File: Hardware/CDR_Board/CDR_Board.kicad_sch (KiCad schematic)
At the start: 60 parts, among them J1 nRF52, J2 nRF24, J3 Battery, J4 GPIO & ADC, J5 USB_C_Receptacle_USB2.0, Q1 DMP2045U, SW1 BOOTSEL, SW2 RESET, SW3 SW_SPDT, U1 W25Q32JVSS, U2 AP2112, U3 RP2040, U4 BQ25172, U6 ADXL343, Y1 Crystal

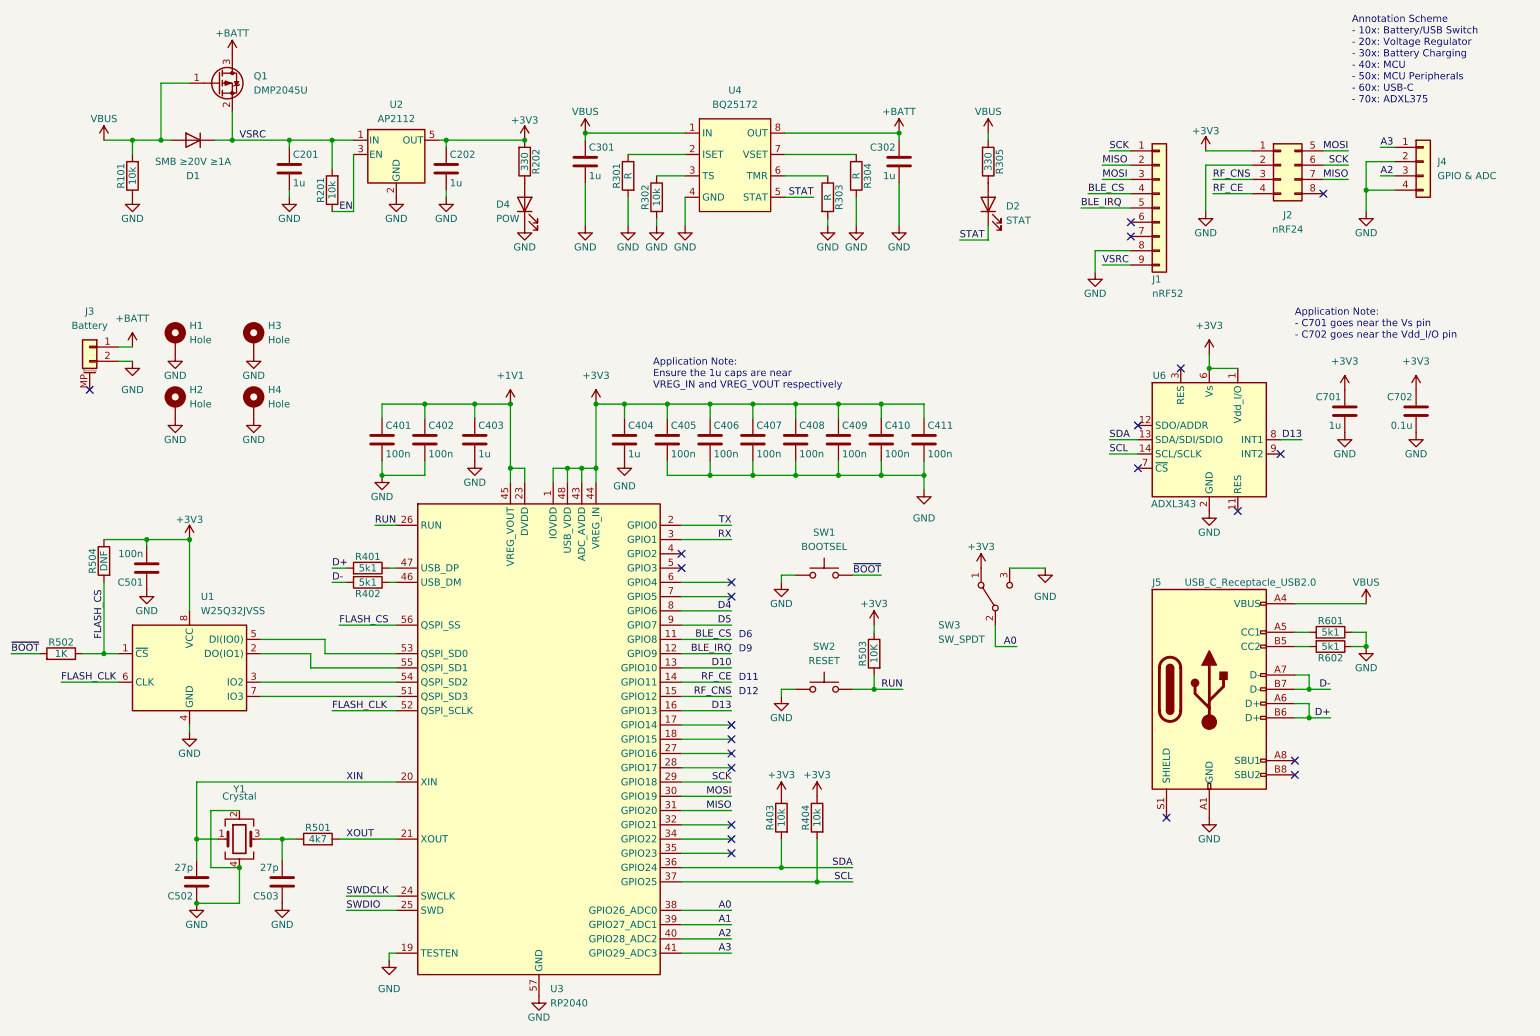
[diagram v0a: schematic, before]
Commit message: Added pullup/pulldown resistors for IMU
Added pullup resistor for CS, pulldown resistor for ADDR pin of IMU. Moved silkscreen
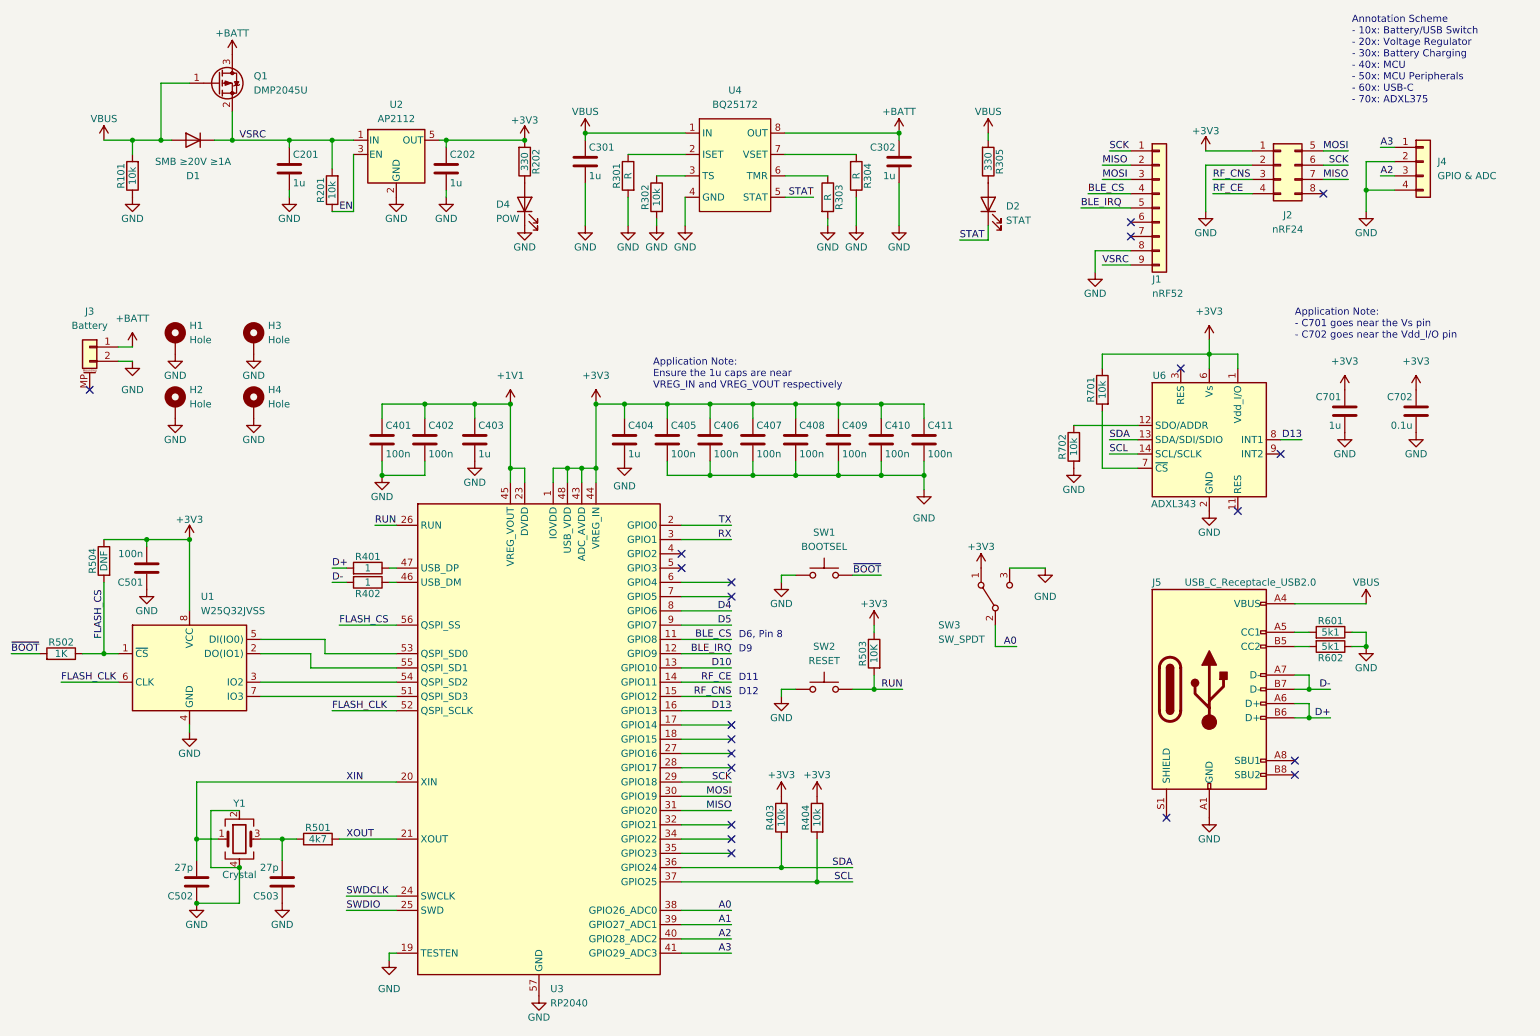
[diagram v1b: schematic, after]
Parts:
- added R701, R702: 10k, Resistor_SMD:R_0805_2012Metric_Pad1.20x1.40mm_HandSolder, symbol Device:R
- R401, R402: value 5k1 -> 1
- Y1: footprint Crystal:Crystal_SMD_0603-4Pin_6.0x3.5mm -> Crystal:Crystal_SMD_SeikoEpson_FA238-4Pin_3.2x2.5mm
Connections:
- net +3V3: now also R701.1
- net GND: now also R702.2
- net at U6.12 (SDO/ADDR): now also R702.1
- net at U6.7 (~{CS}): now also R701.2
- no-connect marks 23 -> 21
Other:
- note added: "D6, Pin 8"
- note removed: "D6"
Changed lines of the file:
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@@
   (junction (at 73.66 38.1) (diameter 0) (color 0 0 0 0)
   )
-  (junction (at 229.87 78.74) (diameter 0) (color 0 0 0 0)
-  )
   (junction (at 140.97 85.09) (diameter 0) (color 0 0 0 0)
   )
@@
   (junction (at 40.64 109.22) (diameter 0) (color 0 0 0 0)
   )
+  (junction (at 229.87 76.2) (diameter 0) (color 0 0 0 0)
+  )
   (junction (at 257.81 46.99) (diameter 0) (color 0 0 0 0)
   )
@@
   (no_connect (at 250.19 47.625))
   (no_connect (at 242.57 93.98))
-  (no_connect (at 217.17 96.52))
-  (no_connect (at 217.17 88.9))
   (no_connect (at 215.9 52.705))
   (no_connect (at 215.9 55.245))
@@
     (stroke (width 0) (type default) (color 0 0 0 0))
   )
+  (wire (pts (xy 210.82 86.36) (xy 210.82 96.52))
+    (stroke (width 0) (type default) (color 0 0 0 0))
+  )
   (wire (pts (xy 245.11 128.27) (xy 247.65 128.27))
     (stroke (width 0) (type default) (color 0 0 0 0))
@@
     (stroke (width 0) (type default) (color 0 0 0 0))
   )
+  (wire (pts (xy 217.17 96.52) (xy 210.82 96.52))
+    (stroke (width 0) (type default) (color 0 0 0 0))
+  )
   (wire (pts (xy 212.09 40.005) (xy 215.9 40.005))
     (stroke (width 0) (type default) (color 0 0 0 0))
@@
     (stroke (width 0) (type default) (color 0 0 0 0))
   )
-  (wire (pts (xy 229.87 78.74) (xy 234.95 78.74))
-    (stroke (width 0) (type default) (color 0 0 0 0))
-  )
   (wire (pts (xy 92.71 38.1) (xy 93.98 38.1))
     (stroke (width 0) (type default) (color 0 0 0 0))
@@
     (stroke (width 0) (type default) (color 0 0 0 0))
   )
+  (wire (pts (xy 210.82 76.2) (xy 229.87 76.2))
+    (stroke (width 0) (type default) (color 0 0 0 0))
+  )
   (wire (pts (xy 82.55 95.25) (xy 82.55 97.79))
     (stroke (width 0) (type default) (color 0 0 0 0))
@@
     (stroke (width 0) (type default) (color 0 0 0 0))
   )
+  (wire (pts (xy 234.95 76.2) (xy 229.87 76.2))
+    (stroke (width 0) (type default) (color 0 0 0 0))
+  )
   (wire (pts (xy 247.65 140.97) (xy 251.46 140.97))
     (stroke (width 0) (type default) (color 0 0 0 0))
   )
+  (wire (pts (xy 205.74 88.9) (xy 217.17 88.9))
+    (stroke (width 0) (type default) (color 0 0 0 0))
+  )
   (wire (pts (xy 257.81 46.99) (xy 257.81 41.91))
     (stroke (width 0) (type default) (color 0 0 0 0))
@@
     (stroke (width 0) (type default) (color 0 0 0 0))
   )
+  (wire (pts (xy 229.87 76.2) (xy 229.87 78.74))
+    (stroke (width 0) (type default) (color 0 0 0 0))
+  )
   (wire (pts (xy 171.45 85.09) (xy 179.07 85.09))
     (stroke (width 0) (type default) (color 0 0 0 0))
@@
     (stroke (width 0) (type default) (color 0 0 0 0))
   )
-  (wire (pts (xy 229.87 76.2) (xy 229.87 78.74))
+  (wire (pts (xy 229.87 73.66) (xy 229.87 76.2))
     (stroke (width 0) (type default) (color 0 0 0 0))
   )
@@
     (stroke (width 0) (type default) (color 0 0 0 0))
   )
+  (wire (pts (xy 234.95 78.74) (xy 234.95 76.2))
+    (stroke (width 0) (type default) (color 0 0 0 0))
+  )
   (wire (pts (xy 247.65 138.43) (xy 247.65 140.97))
     (stroke (width 0) (type default) (color 0 0 0 0))
   )
+  (wire (pts (xy 210.82 78.74) (xy 210.82 76.2))
+    (stroke (width 0) (type default) (color 0 0 0 0))
+  )
   (wire (pts (xy 60.96 137.16) (xy 85.09 137.16))
     (stroke (width 0) (type default) (color 0 0 0 0))
@@
     (stroke (width 0) (type default) (color 0 0 0 0))
   )
-  (text "D6" (at 146.05 127 0)
+  (text "D6, Pin 8\n" (at 146.05 127 0)
     (effects (font (size 1.27 1.27)) (justify left bottom))
   )
@@
     (in_bom yes) (on_board yes)
     (property "Reference" "R402" (id 0) (at 80.01 118.872 90))
-    (property "Value" "5k1" (id 1) (at 80.01 116.84 90))
+    (property "Value" "1" (id 1) (at 80.01 116.84 90))
     (property "Footprint" "Resistor_SMD:R_0805_2012Metric_Pad1.20x1.40mm_HandSolder" (id 2) (at 80.01 115.062 90)
       (effects (font (size 1.27 1.27)) hide)
@@
     (pin "1")
   )
+  (symbol (lib_id "Device:R") (at 210.82 82.55 0) (mirror y) (unit 1)
+    (in_bom yes) (on_board yes)
+    (property "Reference" "R701" (id 0) (at 208.788 82.55 90))
+    (property "Value" "10k" (id 1) (at 210.82 82.55 90))
+    (property "Footprint" "Resistor_SMD:R_0805_2012Metric_Pad1.20x1.40mm_HandSolder" (id 2) (at 212.598 82.55 90)
+      (effects (font (size 1.27 1.27)) hide)
+    )
+    (property "Datasheet" "~" (id 3) (at 210.82 82.55 0)
+      (effects (font (size 1.27 1.27)) hide)
+    )
+    (pin "1")
+    (pin "2")
+  )
   (symbol (lib_id "power:GND") (at 83.82 184.15 0) (unit 1)
     (in_bom yes) (on_board yes) (fields_autoplaced)
@@
     (pin "1")
   )
+  (symbol (lib_id "power:GND") (at 205.74 96.52 0) (mirror y) (unit 1)
+    (in_bom yes) (on_board yes)
+    (property "Reference" "#PWR025" (id 0) (at 205.74 102.87 0)
+      (effects (font (size 1.27 1.27)) hide)
+    )
+    (property "Value" "GND" (id 1) (at 205.74 100.33 0))
+    (property "Footprint" "" (id 2) (at 205.74 96.52 0)
+      (effects (font (size 1.27 1.27)) hide)
+    )
+    (property "Datasheet" "" (id 3) (at 205.74 96.52 0)
+      (effects (font (size 1.27 1.27)) hide)
+    )
+    (pin "1")
+  )
   (symbol (lib_id "Device:R") (at 33.02 113.03 0) (mirror y) (unit 1)
     (in_bom yes) (on_board yes)
@@
   (symbol (lib_id "Device:Crystal_GND24") (at 57.15 162.56 0) (unit 1)
     (in_bom yes) (on_board yes)
-    (property "Reference" "Y1" (id 0) (at 57.15 153.67 0))
-    (property "Value" "Crystal" (id 1) (at 57.15 154.94 0))
-    (property "Footprint" "Crystal:Crystal_SMD_0603-4Pin_6.0x3.5mm" (id 2) (at 57.15 162.56 0)
+    (property "Reference" "Y1" (id 0) (at 57.15 156.21 0))
+    (property "Value" "Crystal" (id 1) (at 57.15 168.91 0))
+    (property "Footprint" "Crystal:Crystal_SMD_SeikoEpson_FA238-4Pin_3.2x2.5mm" (id 2) (at 57.15 162.56 0)
       (effects (font (size 1.27 1.27)) hide)
     )
@@
     (in_bom yes) (on_board yes)
     (property "Reference" "R401" (id 0) (at 80.01 112.268 90))
-    (property "Value" "5k1" (id 1) (at 80.01 114.3 90))
+    (property "Value" "1" (id 1) (at 80.01 114.3 90))
     (property "Footprint" "Resistor_SMD:R_0805_2012Metric_Pad1.20x1.40mm_HandSolder" (id 2) (at 80.01 116.078 90)
       (effects (font (size 1.27 1.27)) hide)
@@
     (pin "1")
   )
-  (symbol (lib_id "power:+3V3") (at 229.87 76.2 0) (unit 1)
+  (symbol (lib_id "power:+3V3") (at 229.87 73.66 0) (unit 1)
     (in_bom yes) (on_board yes) (fields_autoplaced)
-    (property "Reference" "#PWR043" (id 0) (at 229.87 80.01 0)
+    (property "Reference" "#PWR043" (id 0) (at 229.87 77.47 0)
       (effects (font (size 1.27 1.27)) hide)
     )
-    (property "Value" "+3V3" (id 1) (at 229.87 71.12 0))
-    (property "Footprint" "" (id 2) (at 229.87 76.2 0)
+    (property "Value" "+3V3" (id 1) (at 229.87 68.58 0))
+    (property "Footprint" "" (id 2) (at 229.87 73.66 0)
       (effects (font (size 1.27 1.27)) hide)
     )
-    (property "Datasheet" "" (id 3) (at 229.87 76.2 0)
+    (property "Datasheet" "" (id 3) (at 229.87 73.66 0)
       (effects (font (size 1.27 1.27)) hide)
     )
@@
     (pin "2")
   )
+  (symbol (lib_id "Device:R") (at 205.74 92.71 0) (mirror y) (unit 1)
+    (in_bom yes) (on_board yes)
+    (property "Reference" "R702" (id 0) (at 203.708 92.71 90))
+    (property "Value" "10k" (id 1) (at 205.74 92.71 90))
+    (property "Footprint" "Resistor_SMD:R_0805_2012Metric_Pad1.20x1.40mm_HandSolder" (id 2) (at 207.518 92.71 90)
+      (effects (font (size 1.27 1.27)) hide)
+    )
+    (property "Datasheet" "~" (id 3) (at 205.74 92.71 0)
+      (effects (font (size 1.27 1.27)) hide)
+    )
+    (pin "1")
+    (pin "2")
+  )
   (symbol (lib_id "Mechanical:MountingHole_Pad") (at 45.72 85.09 0) (unit 1)
     (in_bom yes) (on_board yes) (fields_autoplaced)
@@
       (reference "#PWR024") (unit 1) (value "GND") (footprint "")
     )
+    (path "/81239117-23b7-4c49-b0b2-240763e68c7c"
+      (reference "#PWR025") (unit 1) (value "GND") (footprint "")
+    )
     (path "/3f8e544f-af80-4d36-b24c-7af3fe033ca7"
       (reference "#PWR026") (unit 1) (value "+3V3") (footprint "")
@@
     )
     (path "/a2f80b76-0769-4b67-b20b-5b97e454ee5d"
-      (reference "R401") (unit 1) (value "5k1") (footprint "Resistor_SMD:R_0805_2012Metric_Pad1.20x1.40mm_HandSolder")
+      (reference "R401") (unit 1) (value "1") (footprint "Resistor_SMD:R_0805_2012Metric_Pad1.20x1.40mm_HandSolder")
     )
     (path "/202cef2a-53d4-4947-b0f5-0c8f386934f3"
-      (reference "R402") (unit 1) (value "5k1") (footprint "Resistor_SMD:R_0805_2012Metric_Pad1.20x1.40mm_HandSolder")
+      (reference "R402") (unit 1) (value "1") (footprint "Resistor_SMD:R_0805_2012Metric_Pad1.20x1.40mm_HandSolder")
     )
     (path "/dae6396c-3993-43e0-8d42-762eadb57d2a"
@@
       (reference "R602") (unit 1) (value "5k1") (footprint "Resistor_SMD:R_0805_2012Metric_Pad1.20x1.40mm_HandSolder")
     )
+    (path "/4a17b071-e449-43c8-8002-f0161ec89edf"
+      (reference "R701") (unit 1) (value "10k") (footprint "Resistor_SMD:R_0805_2012Metric_Pad1.20x1.40mm_HandSolder")
+    )
+    (path "/daffb66f-2c1d-4343-aca4-a84d0a0726fe"
+      (reference "R702") (unit 1) (value "10k") (footprint "Resistor_SMD:R_0805_2012Metric_Pad1.20x1.40mm_HandSolder")
+    )
     (path "/e27b1634-eb06-4322-aa5f-8515e8e7bec4"
       (reference "SW1") (unit 1) (value "BOOTSEL") (footprint "Button_Switch_SMD:SW_Push_1P1T_NO_CK_KMR2")
@@
     )
     (path "/995eeaa6-72b4-4903-ad90-fb782bcfdcb1"
-      (reference "Y1") (unit 1) (value "Crystal") (footprint "Crystal:Crystal_SMD_0603-4Pin_6.0x3.5mm")
+      (reference "Y1") (unit 1) (value "Crystal") (footprint "Crystal:Crystal_SMD_SeikoEpson_FA238-4Pin_3.2x2.5mm")
     )
   )
